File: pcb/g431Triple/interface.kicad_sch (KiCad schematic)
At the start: 32 parts, among them P4 har-flexicon 2,54 MSH-4, P5 har-flexicon 2,54 MSH-4, P6 har-flexicon 2,54 MSH-4, P7 WAGO2061-602, P8 WAGO2061-602, P9 WAGO2061-602, U4 SP3485CN, U5 SP3485CN, U6 SP3485CN

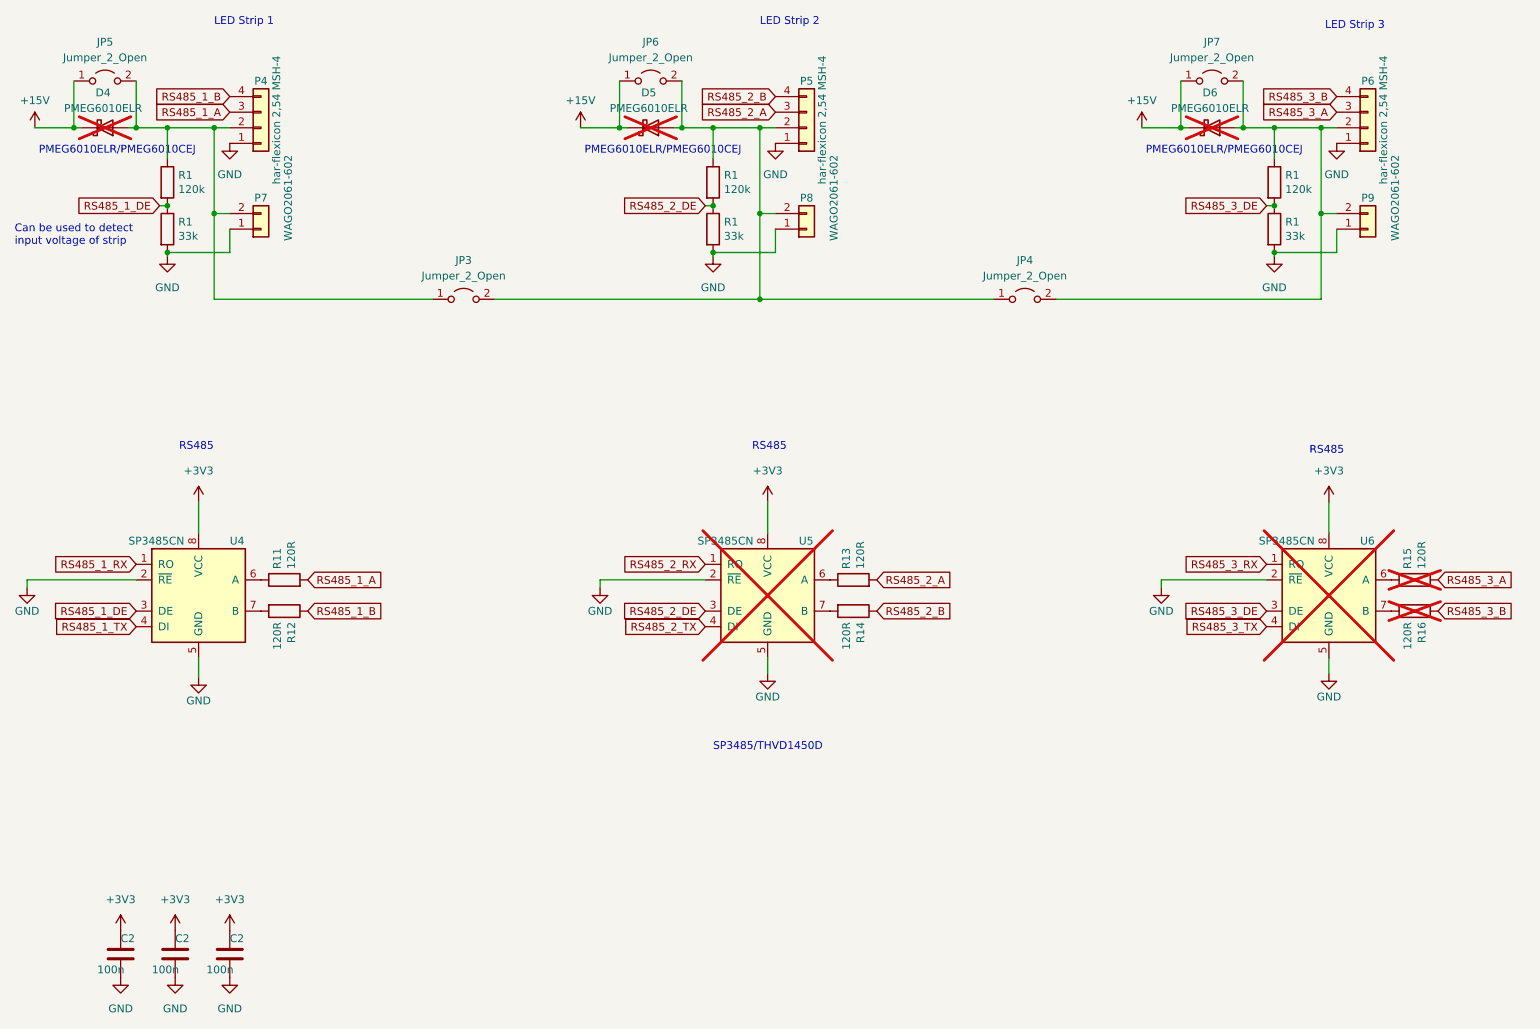
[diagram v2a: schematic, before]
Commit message: Start preset name editor
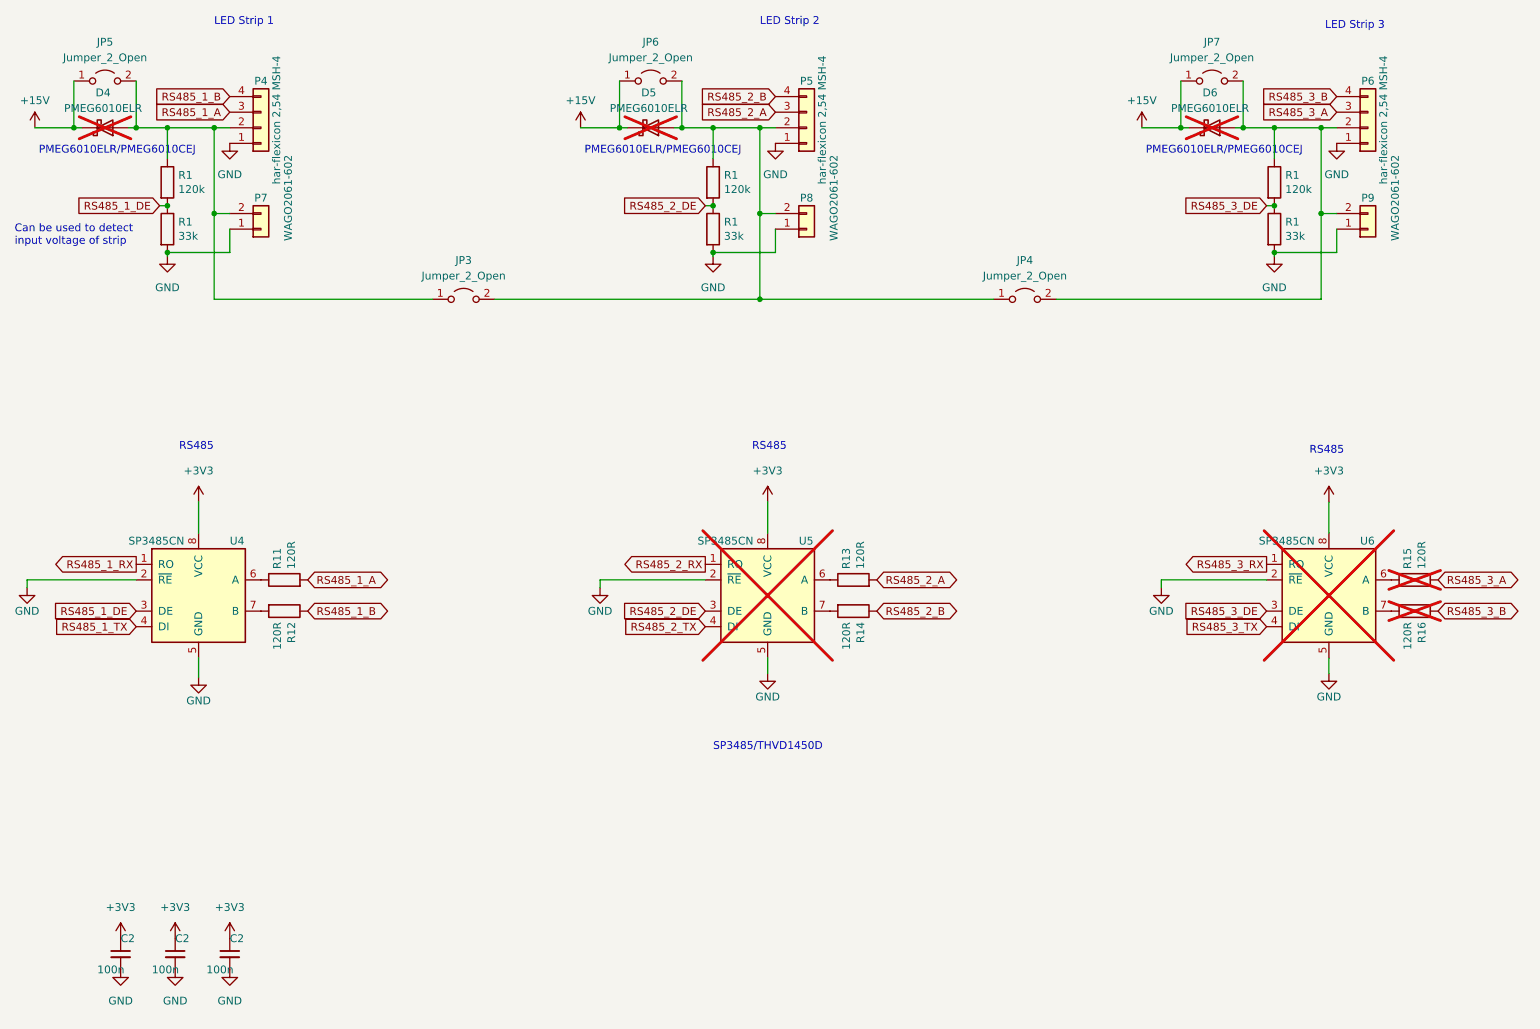
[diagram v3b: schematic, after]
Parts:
- C2: symbol Device:C -> Device:C_Small
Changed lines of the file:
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@@
 	)
 	(global_label "RS485_1_B"
-		(shape input)
+		(shape bidirectional)
 		(at 67.31 124.46 0)
 		(effects
@@
 	)
 	(global_label "RS485_3_B"
-		(shape input)
+		(shape bidirectional)
 		(at 251.46 124.46 0)
 		(effects
@@
 	)
 	(global_label "RS485_2_B"
-		(shape input)
+		(shape bidirectional)
 		(at 160.02 124.46 0)
 		(effects
@@
 	)
 	(global_label "RS485_2_RX"
-		(shape input)
+		(shape output)
 		(at 132.08 116.84 180)
 		(effects
@@
 	)
 	(global_label "RS485_1_A"
-		(shape input)
+		(shape bidirectional)
 		(at 67.31 119.38 0)
 		(effects
@@
 	)
 	(global_label "RS485_3_A"
-		(shape input)
+		(shape bidirectional)
 		(at 251.46 119.38 0)
 		(effects
@@
 	)
 	(global_label "RS485_2_A"
-		(shape input)
+		(shape bidirectional)
 		(at 160.02 119.38 0)
 		(effects
@@
 	)
 	(global_label "RS485_1_RX"
-		(shape input)
+		(shape output)
 		(at 39.37 116.84 180)
 		(effects
@@
 	)
 	(global_label "RS485_3_RX"
-		(shape input)
+		(shape output)
 		(at 223.52 116.84 180)
 		(effects
@@
 	)
 	(symbol
-		(lib_id "Device:C")
+		(lib_id "Device:C_Small")
 		(at 45.72 180.34 0)
 		(unit 1)
@@
 		)
 		(property "Footprint" "local:0603"
-			(at 46.6852 184.15 0)
+			(at 45.72 180.34 0)
 			(effects
 				(font
@@
 			)
 		)
-		(property "Description" ""
+		(property "Description" "Unpolarized capacitor, small symbol"
 			(at 45.72 180.34 0)
 			(effects
@@
 	(symbol
 		(lib_id "power:GND")
-		(at 54.61 184.15 0)
+		(at 54.61 182.88 0)
 		(unit 1)
 		(exclude_from_sim no)
@@
 		(fields_autoplaced yes)
 		(property "Reference" "#PWR010"
-			(at 54.61 190.5 0)
+			(at 54.61 189.23 0)
 			(effects
 				(font
@@
 		)
 		(property "Value" "GND"
-			(at 54.61 189.23 0)
+			(at 54.61 187.96 0)
 			(effects
 				(font
@@
 		)
 		(property "Footprint" ""
-			(at 54.61 184.15 0)
+			(at 54.61 182.88 0)
 			(effects
 				(font
@@
 		)
 		(property "Datasheet" ""
-			(at 54.61 184.15 0)
+			(at 54.61 182.88 0)
 			(effects
 				(font
@@
 		)
 		(property "Description" ""
-			(at 54.61 184.15 0)
+			(at 54.61 182.88 0)
 			(effects
 				(font
@@
 	)
 	(symbol
-		(lib_id "Device:C")
+		(lib_id "Device:C_Small")
 		(at 36.83 180.34 0)
 		(unit 1)
@@
 		)
 		(property "Footprint" "local:0603"
-			(at 37.7952 184.15 0)
+			(at 36.83 180.34 0)
 			(effects
 				(font
@@
 			)
 		)
-		(property "Description" ""
+		(property "Description" "Unpolarized capacitor, small symbol"
 			(at 36.83 180.34 0)
 			(effects
@@
 	)
 	(symbol
-		(lib_id "Device:C")
+		(lib_id "Device:C_Small")
 		(at 54.61 180.34 0)
 		(unit 1)
@@
 		)
 		(property "Footprint" "local:0603"
-			(at 55.5752 184.15 0)
+			(at 54.61 180.34 0)
 			(effects
 				(font
@@
 			)
 		)
-		(property "Description" ""
+		(property "Description" "Unpolarized capacitor, small symbol"
 			(at 54.61 180.34 0)
 			(effects
@@
 	(symbol
 		(lib_id "power:+3V3")
-		(at 45.72 176.53 0)
+		(at 45.72 177.8 0)
 		(unit 1)
 		(exclude_from_sim no)
@@
 		(fields_autoplaced yes)
 		(property "Reference" "#PWR09"
-			(at 45.72 180.34 0)
+			(at 45.72 181.61 0)
 			(effects
 				(font
@@
 		)
 		(property "Value" "+3V3"
-			(at 45.72 171.45 0)
+			(at 45.72 172.72 0)
 			(effects
 				(font
@@
 		)
 		(property "Footprint" ""
-			(at 45.72 176.53 0)
+			(at 45.72 177.8 0)
 			(effects
 				(font
@@
 		)
 		(property "Datasheet" ""
-			(at 45.72 176.53 0)
+			(at 45.72 177.8 0)
 			(effects
 				(font
@@
 		)
 		(property "Description" ""
-			(at 45.72 176.53 0)
+			(at 45.72 177.8 0)
 			(effects
 				(font
@@
 	(symbol
 		(lib_id "power:GND")
-		(at 45.72 184.15 0)
+		(at 45.72 182.88 0)
 		(unit 1)
 		(exclude_from_sim no)
@@
 		(fields_autoplaced yes)
 		(property "Reference" "#PWR010"
-			(at 45.72 190.5 0)
+			(at 45.72 189.23 0)
 			(effects
 				(font
@@
 		)
 		(property "Value" "GND"
-			(at 45.72 189.23 0)
+			(at 45.72 187.96 0)
 			(effects
 				(font
@@
 		)
 		(property "Footprint" ""
-			(at 45.72 184.15 0)
+			(at 45.72 182.88 0)
 			(effects
 				(font
@@
 		)
 		(property "Datasheet" ""
-			(at 45.72 184.15 0)
+			(at 45.72 182.88 0)
 			(effects
 				(font
@@
 		)
 		(property "Description" ""
-			(at 45.72 184.15 0)
+			(at 45.72 182.88 0)
 			(effects
 				(font
@@
 	(symbol
 		(lib_id "power:+3V3")
-		(at 36.83 176.53 0)
+		(at 36.83 177.8 0)
 		(unit 1)
 		(exclude_from_sim no)
@@
 		(fields_autoplaced yes)
 		(property "Reference" "#PWR09"
-			(at 36.83 180.34 0)
+			(at 36.83 181.61 0)
 			(effects
 				(font
@@
 		)
 		(property "Value" "+3V3"
-			(at 36.83 171.45 0)
+			(at 36.83 172.72 0)
 			(effects
 				(font
@@
 		)
 		(property "Footprint" ""
-			(at 36.83 176.53 0)
+			(at 36.83 177.8 0)
 			(effects
 				(font
@@
 		)
 		(property "Datasheet" ""
-			(at 36.83 176.53 0)
+			(at 36.83 177.8 0)
 			(effects
 				(font
@@
 		)
 		(property "Description" ""
-			(at 36.83 176.53 0)
+			(at 36.83 177.8 0)
 			(effects
 				(font
@@
 	(symbol
 		(lib_id "power:GND")
-		(at 36.83 184.15 0)
+		(at 36.83 182.88 0)
 		(unit 1)
 		(exclude_from_sim no)
@@
 		(fields_autoplaced yes)
 		(property "Reference" "#PWR010"
-			(at 36.83 190.5 0)
+			(at 36.83 189.23 0)
 			(effects
 				(font
@@
 		)
 		(property "Value" "GND"
-			(at 36.83 189.23 0)
+			(at 36.83 187.96 0)
 			(effects
 				(font
@@
 		)
 		(property "Footprint" ""
-			(at 36.83 184.15 0)
+			(at 36.83 182.88 0)
 			(effects
 				(font
@@
 		)
 		(property "Datasheet" ""
-			(at 36.83 184.15 0)
+			(at 36.83 182.88 0)
 			(effects
 				(font
@@
 		)
 		(property "Description" ""
-			(at 36.83 184.15 0)
+			(at 36.83 182.88 0)
 			(effects
 				(font
@@
 	(symbol
 		(lib_id "power:+3V3")
-		(at 54.61 176.53 0)
+		(at 54.61 177.8 0)
 		(unit 1)
 		(exclude_from_sim no)
@@
 		(fields_autoplaced yes)
 		(property "Reference" "#PWR09"
-			(at 54.61 180.34 0)
+			(at 54.61 181.61 0)
 			(effects
 				(font
@@
 		)
 		(property "Value" "+3V3"
-			(at 54.61 171.45 0)
+			(at 54.61 172.72 0)
 			(effects
 				(font
@@
 		)
 		(property "Footprint" ""
-			(at 54.61 176.53 0)
+			(at 54.61 177.8 0)
 			(effects
 				(font
@@
 		)
 		(property "Datasheet" ""
-			(at 54.61 176.53 0)
+			(at 54.61 177.8 0)
 			(effects
 				(font
@@
 		)
 		(property "Description" ""
-			(at 54.61 176.53 0)
+			(at 54.61 177.8 0)
 			(effects
 				(font

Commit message: Works on g431Triple
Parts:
- renumbered C2 to C16, C2 to C17, C2 to C18, R1 to R10, R1 to R5, R1 to R6, R1 to R7, R1 to R8, R1 to R9
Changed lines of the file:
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@@
 (kicad_sch
-	(version 20231120)
+	(version 20250114)
 	(generator "eeschema")
-	(generator_version "8.0")
+	(generator_version "9.0")
 	(paper "A4")
+	(text "Can be used to detect\ninput voltage of strip"
+		(exclude_from_sim no)
+		(at 19.558 65.024 0)
+		(effects
+			(font
+				(size 1.27 1.27)
+			)
+			(justify left bottom)
+		)
+	)
+	(text "LED Strip 3"
+		(exclude_from_sim no)
+		(at 233.045 29.845 0)
+		(effects
+			(font
+				(size 1.27 1.27)
+			)
+			(justify left bottom)
+		)
+	)
+	(text "PMEG6010ELR/PMEG6010CEJ "
+		(exclude_from_sim no)
+		(at 112.395 50.165 0)
+		(effects
+			(font
+				(size 1.27 1.27)
+			)
+			(justify left bottom)
+		)
+	)
+	(text "LED Strip 1"
+		(exclude_from_sim no)
+		(at 52.07 29.21 0)
+		(effects
+			(font
+				(size 1.27 1.27)
+			)
+			(justify left bottom)
+		)
+	)
+	(text "SP3485/THVD1450D"
+		(exclude_from_sim no)
+		(at 133.35 147.32 0)
+		(effects
+			(font
+				(size 1.27 1.27)
+			)
+			(justify left bottom)
+		)
+	)
+	(text "LED Strip 2"
+		(exclude_from_sim no)
+		(at 140.97 29.21 0)
+		(effects
+			(font
+				(size 1.27 1.27)
+			)
+			(justify left bottom)
+		)
+	)
+	(text "PMEG6010ELR/PMEG6010CEJ "
+		(exclude_from_sim no)
+		(at 23.495 50.165 0)
+		(effects
+			(font
+				(size 1.27 1.27)
+			)
+			(justify left bottom)
+		)
+	)
+	(text "RS485"
+		(exclude_from_sim no)
+		(at 230.505 99.06 0)
+		(effects
+			(font
+				(size 1.27 1.27)
+			)
+			(justify left bottom)
+		)
+	)
+	(text "RS485"
+		(exclude_from_sim no)
+		(at 46.355 98.425 0)
+		(effects
+			(font
+				(size 1.27 1.27)
+			)
+			(justify left bottom)
+		)
+	)
+	(text "PMEG6010ELR/PMEG6010CEJ "
+		(exclude_from_sim no)
+		(at 203.835 50.165 0)
+		(effects
+			(font
+				(size 1.27 1.27)
+			)
+			(justify left bottom)
+		)
+	)
+	(text "RS485"
+		(exclude_from_sim no)
+		(at 139.7 98.425 0)
+		(effects
+			(font
+				(size 1.27 1.27)
+			)
+			(justify left bottom)
+		)
+	)
 	(junction
 		(at 140.97 73.66)
@@
 		)
 	)
-	(text "Can be used to detect\ninput voltage of strip"
-		(exclude_from_sim no)
-		(at 19.558 65.024 0)
-		(effects
-			(font
-				(size 1.27 1.27)
-			)
-			(justify left bottom)
-		)
-	)
-	(text "LED Strip 3"
-		(exclude_from_sim no)
-		(at 233.045 29.845 0)
-		(effects
-			(font
-				(size 1.27 1.27)
-			)
-			(justify left bottom)
-		)
-	)
-	(text "PMEG6010ELR/PMEG6010CEJ "
-		(exclude_from_sim no)
-		(at 112.395 50.165 0)
-		(effects
-			(font
-				(size 1.27 1.27)
-			)
-			(justify left bottom)
-		)
-	)
-	(text "LED Strip 1"
-		(exclude_from_sim no)
-		(at 52.07 29.21 0)
-		(effects
-			(font
-				(size 1.27 1.27)
-			)
-			(justify left bottom)
-		)
-	)
-	(text "SP3485/THVD1450D"
-		(exclude_from_sim no)
-		(at 133.35 147.32 0)
-		(effects
-			(font
-				(size 1.27 1.27)
-			)
-			(justify left bottom)
-		)
-	)
-	(text "LED Strip 2"
-		(exclude_from_sim no)
-		(at 140.97 29.21 0)
-		(effects
-			(font
-				(size 1.27 1.27)
-			)
-			(justify left bottom)
-		)
-	)
-	(text "PMEG6010ELR/PMEG6010CEJ "
-		(exclude_from_sim no)
-		(at 23.495 50.165 0)
-		(effects
-			(font
-				(size 1.27 1.27)
-			)
-			(justify left bottom)
-		)
-	)
-	(text "RS485"
-		(exclude_from_sim no)
-		(at 230.505 99.06 0)
-		(effects
-			(font
-				(size 1.27 1.27)
-			)
-			(justify left bottom)
-		)
-	)
-	(text "RS485"
-		(exclude_from_sim no)
-		(at 46.355 98.425 0)
-		(effects
-			(font
-				(size 1.27 1.27)
-			)
-			(justify left bottom)
-		)
-	)
-	(text "PMEG6010ELR/PMEG6010CEJ "
-		(exclude_from_sim no)
-		(at 203.835 50.165 0)
-		(effects
-			(font
-				(size 1.27 1.27)
-			)
-			(justify left bottom)
-		)
-	)
-	(text "RS485"
-		(exclude_from_sim no)
-		(at 139.7 98.425 0)
-		(effects
-			(font
-				(size 1.27 1.27)
-			)
-			(justify left bottom)
-		)
-	)
 	(global_label "RS485_3_TX"
 		(shape input)
@@
 		(dnp no)
 		(fields_autoplaced yes)
-		(property "Reference" "#PWR010"
+		(property "Reference" "#PWR046"
 			(at 234.95 54.61 0)
 			(effects
@@
 		(on_board yes)
 		(dnp no)
-		(property "Reference" "R1"
+		(property "Reference" "R6"
 			(at 46.228 61.0616 0)
 			(effects
@@
 		(on_board yes)
 		(dnp no)
-		(property "Reference" "C2"
+		(property "Reference" "C17"
 			(at 45.72 177.8 0)
 			(effects
@@
 		(dnp no)
 		(fields_autoplaced yes)
-		(property "Reference" "#PWR010"
+		(property "Reference" "#PWR051"
 			(at 54.61 189.23 0)
 			(effects
@@
 		(dnp no)
 		(fields_autoplaced yes)
-		(property "Reference" "#PWR010"
+		(property "Reference" "#PWR014"
 			(at 143.51 54.61 0)
 			(effects
@@
 		(dnp no)
 		(fields_autoplaced yes)
-		(property "Reference" "#PWR02"
+		(property "Reference" "#PWR040"
 			(at 233.68 110.49 0)
 			(effects
@@
 		(on_board yes)
 		(dnp no)
-		(property "Reference" "C2"
+		(property "Reference" "C16"
 			(at 36.83 177.8 0)
 			(effects
@@
 		(dnp no)
 		(fields_autoplaced yes)
-		(property "Reference" "#PWR010"
+		(property "Reference" "#PWR044"
 			(at 44.45 73.025 0)
 			(effects
@@
 		(dnp no)
 		(fields_autoplaced yes)
-		(property "Reference" "#PWR02"
+		(property "Reference" "#PWR036"
 			(at 49.53 110.49 0)
 			(effects
@@
 		(dnp no)
 		(fields_autoplaced yes)
-		(property "Reference" "#PWR02"
+		(property "Reference" "#PWR039"
 			(at 142.24 110.49 0)
 			(effects
@@
 		(on_board yes)
 		(dnp no)
-		(property "Reference" "R1"
+		(property "Reference" "R5"
 			(at 46.228 53.4416 0)
 			(effects
@@
 		(dnp no)
 		(fields_autoplaced yes)
-		(property "Reference" "#PWR010"
+		(property "Reference" "#PWR035"
 			(at 133.35 73.025 0)
 			(effects
@@
 		(on_board yes)
 		(dnp no)
-		(property "Reference" "C2"
+		(property "Reference" "C18"
 			(at 54.61 177.8 0)
 			(effects
@@
 		(on_board yes)
 		(dnp no)
-		(property "Reference" "R1"
+		(property "Reference" "R10"
 			(at 226.568 61.0616 0)
 			(effects
@@
 		(on_board yes)
 		(dnp no)
-		(property "Reference" "R1"
+		(property "Reference" "R9"
 			(at 226.568 53.4416 0)
 			(effects
@@
 		(dnp no)
 		(fields_autoplaced yes)
-		(property "Reference" "#PWR09"
+		(property "Reference" "#PWR048"
 			(at 45.72 181.61 0)
 			(effects
@@
 		(dnp no)
 		(fields_autoplaced yes)
-		(property "Reference" "#PWR010"
+		(property "Reference" "#PWR049"
 			(at 45.72 189.23 0)
 			(effects
@@
 		(dnp no)
 		(fields_autoplaced yes)
-		(property "Reference" "#PWR010"
+		(property "Reference" "#PWR043"
 			(at 54.61 54.61 0)
 			(effects
@@
 		(on_board yes)
 		(dnp no)
-		(property "Reference" "R1"
+		(property "Reference" "R7"
 			(at 135.128 53.4416 0)
 			(effects
@@
 		(on_board yes)
 		(dnp no)
-		(property "Reference" "R1"
+		(property "Reference" "R8"
 			(at 135.128 61.0616 0)
 			(effects
@@
 		(dnp no)
 		(fields_autoplaced yes)
-		(property "Reference" "#PWR09"
+		(property "Reference" "#PWR050"
 			(at 54.61 181.61 0)
 			(effects
@@
 		(dnp no)
 		(fields_autoplaced yes)
-		(property "Reference" "#PWR010"
+		(property "Reference" "#PWR047"
 			(at 224.79 73.025 0)
 			(effects
